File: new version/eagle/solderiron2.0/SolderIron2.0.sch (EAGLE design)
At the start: 7 parts

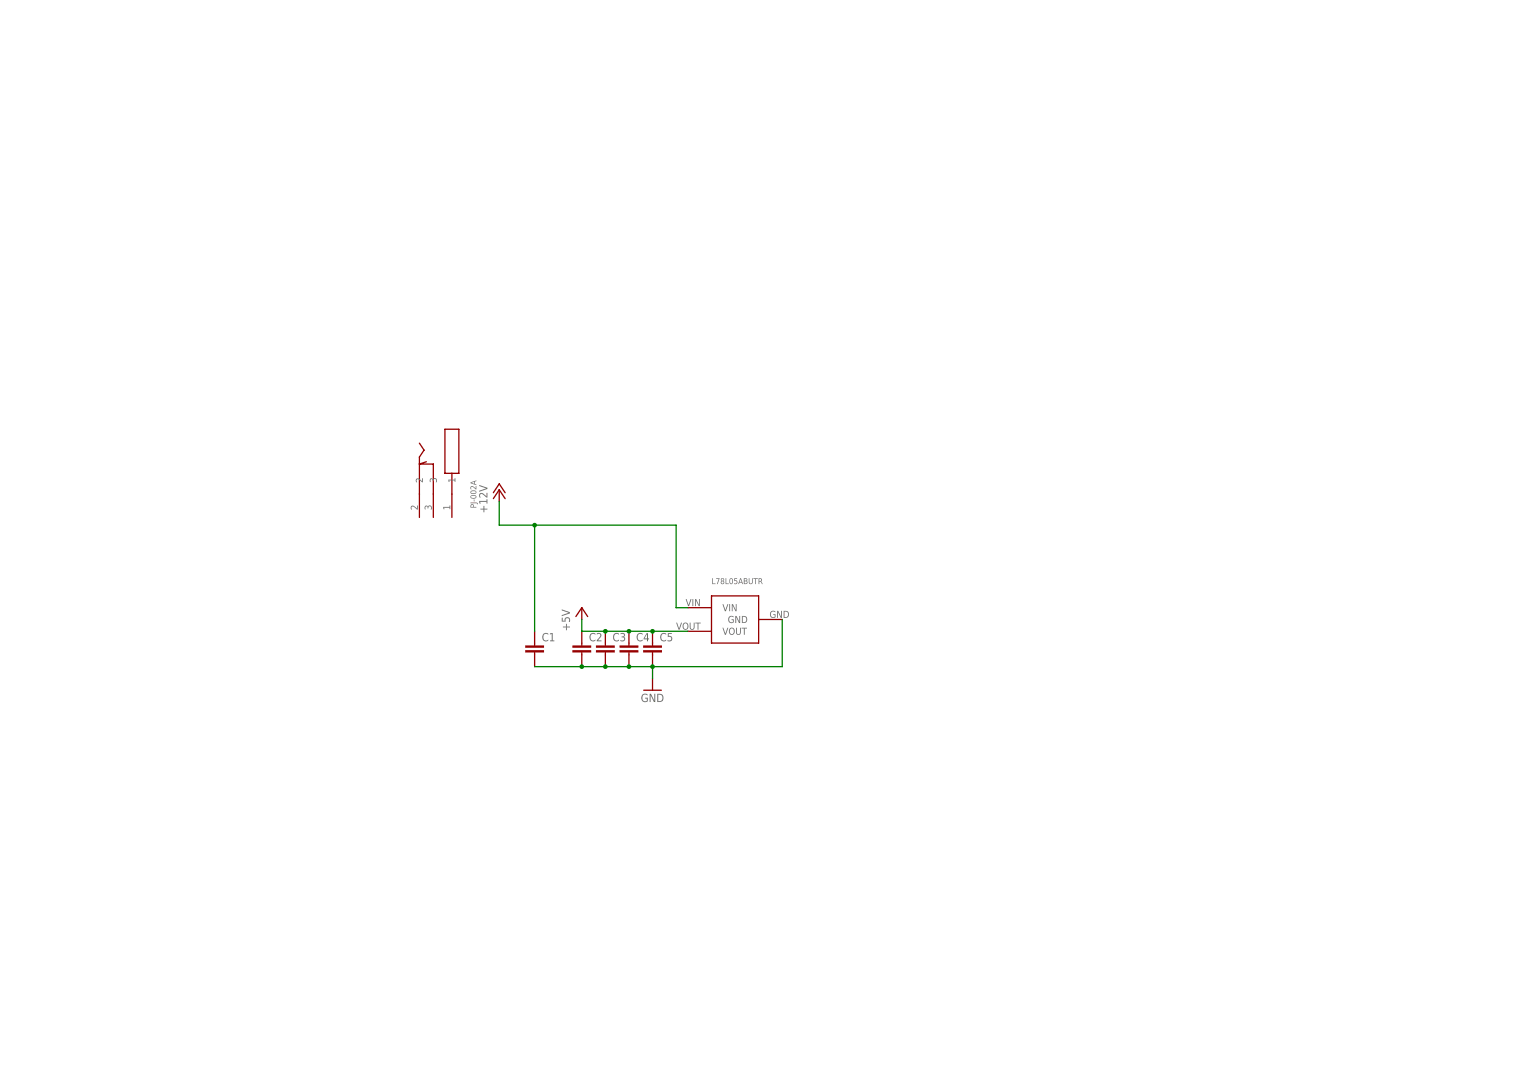
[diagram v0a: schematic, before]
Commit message: created eagle schematics
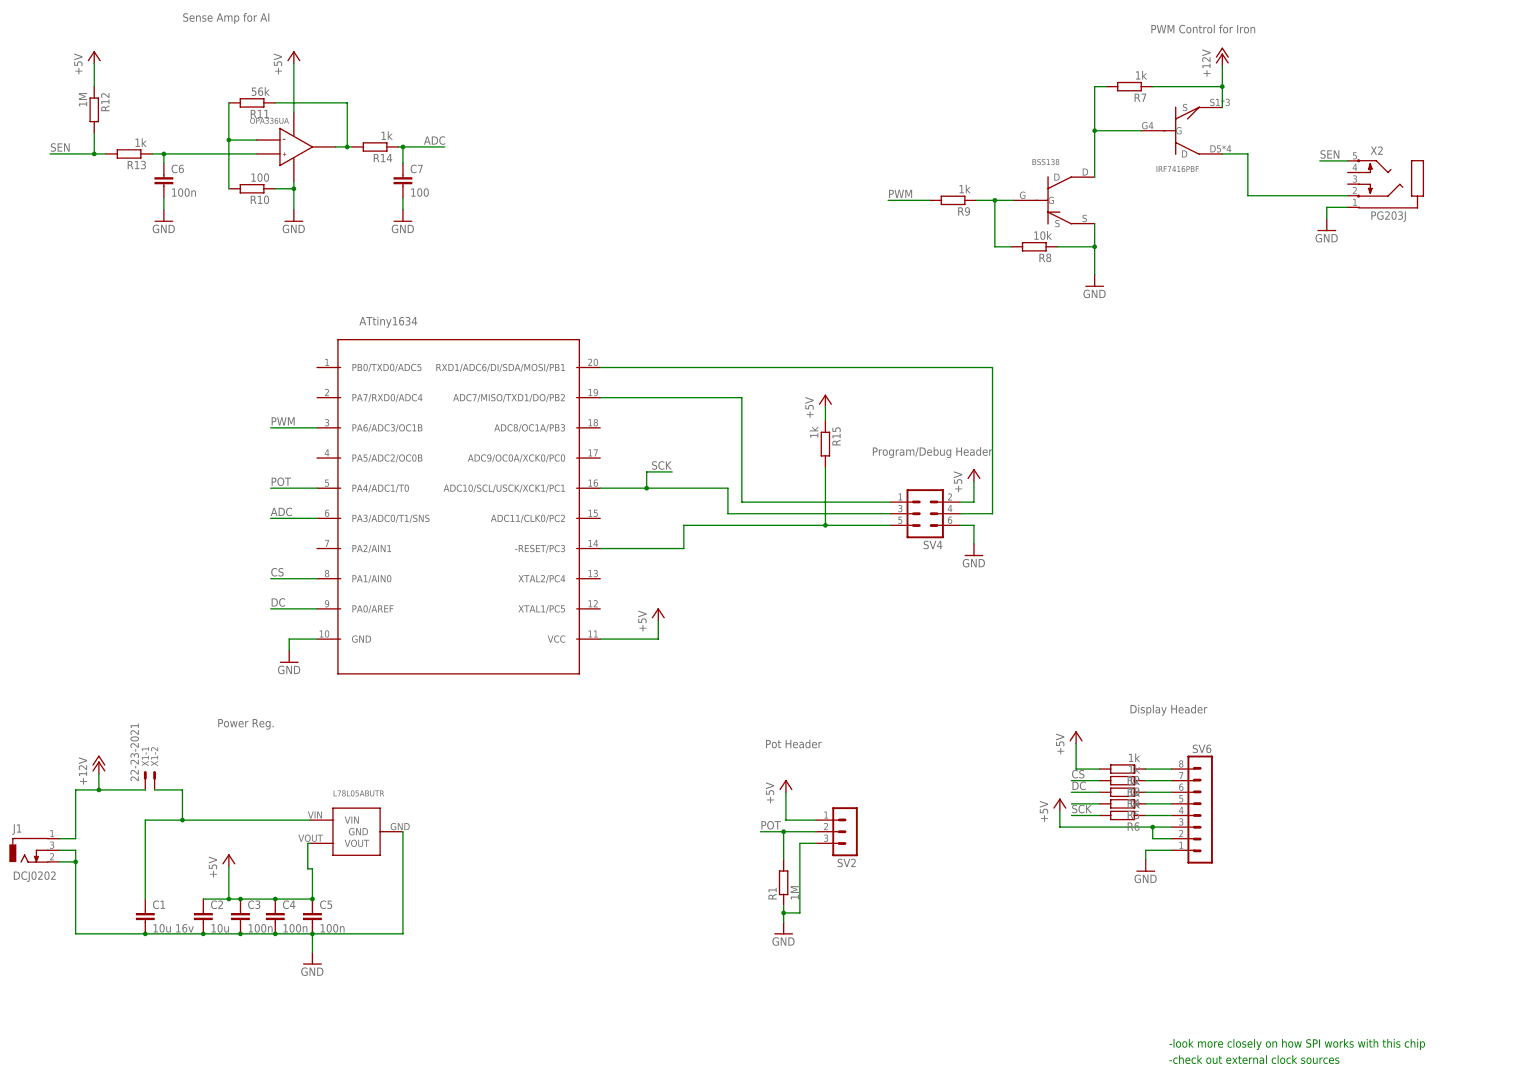
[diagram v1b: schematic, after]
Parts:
- added C6: 100n, eagle-ltspice:CC1206
- added C7: 100, eagle-ltspice:CC1206
- added J1: DCJ0202, solderstation:DCJ0202
- added R1, R12: 1M, eagle-ltspice:RR0603
- added R10: 100, eagle-ltspice:RR0603
- added R11: 56k, eagle-ltspice:RR0603
- added R13, R14, R15, R2, R3, R4, R5, R6, R7, R9: 1k, eagle-ltspice:RR0603
- added R8: 10k, eagle-ltspice:RR0603
- added SV2: (no value), con-lstb:MA03-1
- added SV4: (no value), con-lstb:MA03-2
- added SV6: (no value), con-lstb:MA08-1
- added U$3: BSS138, solderstation:BSS138
- added U$4: OPA336UA, solderstation:OPA336UA
- added U$5: ATTINY1634, solderstation:ATTINY1634
- added X1: 22-23-2021, con-molex:22-23-2021
- added X2: PG203J, solderstation:PG203J
- C1: value (none) -> 10u 16v
- C2: value (none) -> 10u
- C3, C4, C5: value (none) -> 100n
- U$1: value PJ-002A -> IRF7416PBF; device solderstation:PJ-002A -> solderstation:IRF7416PBF
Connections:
- new net ADC: C7.1, R14.1, U$5.PA3/ADC0/T1/SNS
- new net CS: R3.2, U$5.PA1/AIN0
- new net DC: R4.2, U$5.PA0/AREF
- new net MOSI: SV4.1, U$5.ADC7/MISO/TXD1/DO/PB2
- new net N$10: R8.2, R9.1, U$3.G
- new net N$11: R10.2, R11.2, U$4.IN-
- new net N$12: R11.1, R14.2, U$4.OUTPUT
- new net N$13: C6.1, R13.1, U$4.IN+
- new net N$17: SV4.4, U$5.RXD1/ADC6/DI/SDA/MOSI/PB1
- new net N$19: R15.2, SV4.5, U$5.-RESET/PC3
- new net N$2: R2.1, SV6.8
- new net N$23: R5.2
- new net N$3: C1.1, U$2.VIN, X1-2.S
- new net N$4: R3.1, SV6.7
- new net N$5: R4.1, SV6.6
- new net N$6: R5.1, SV6.5
- new net N$7: R6.1, SV6.4
- new net N$8: U$1.D, X2.2
- new net N$9: R7.2, U$1.G, U$3.D
- new net POT: R1.2, SV2.2, U$5.PA4/ADC1/T0
- new net PWM: R9.2, U$5.PA6/ADC3/OC1B
- new net SCK: R6.2, SV4.3, U$5.ADC10/SCL/USCK/XCK1/PC1
- new net SEN: R12.2, R13.2, X2.5
- net +12V: now also J1.1, R7.1, U$1.S; no longer C1.1, U$2.VIN
- net +5V: now also R12.1, R15.1, R2.2, SV2.1, SV4.2, SV6.2, SV6.3, U$4.V+, U$5.VCC
- net GND: now also C6.2, C7.2, J1.2, J1.3, R1.1, R10.1, R8.1, SV2.3, SV4.6, SV6.1, U$3.S, U$4.V-, U$5.GND, X2.1
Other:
- note added: "-check out external clock sources"
- note added: "-look more closely on how SPI works with this chip"
- note added: "Display Header"
- note added: "PWM Control for Iron"
- note added: "Pot Header"
- note added: "Power Reg."
- note added: "Program/Debug Header"
- note added: "Sense Amp for AI"
- moved on the sheet: C1, C2, C3, C4, C5

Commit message: finished v2 schematic
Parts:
- added C8, C9: 22p, eagle-ltspice:CC1206
- added U$6: CX3225GB12000H0KPSC1, solderstation:CX3225GB12000H0KPSC1
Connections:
- removed net N$17: SV4.4, U$5.RXD1/ADC6/DI/SDA/MOSI/PB1
- removed net N$23: R5.2
- new net N$1: C8.1, U$5.XTAL2/PC4, U$6.2
- new net N$14: C9.1, U$5.XTAL1/PC5, U$6.1
- net GND: now also C8.2, C9.2
- net MOSI: now also R5.2, SV4.4, U$5.RXD1/ADC6/DI/SDA/MOSI/PB1
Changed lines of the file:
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@@
 <part name="P+11" library="supply1" deviceset="+5V" device=""/>
 <part name="GND10" library="supply1" deviceset="GND" device=""/>
+<part name="U$6" library="solderstation" deviceset="CX3225GB12000H0KPSC1" device=""/>
+<part name="C8" library="eagle-ltspice" deviceset="C" device="C1206" value="22p"/>
+<part name="C9" library="eagle-ltspice" deviceset="C" device="C1206" value="22p"/>
+<part name="GND11" library="supply1" deviceset="GND" device=""/>
 </parts>
 <sheets>
@@
 <instance part="P+11" gate="1" x="-14" y="-15.5"/>
 <instance part="GND10" gate="1" x="-93.5" y="-27"/>
+<instance part="U$6" gate="G$1" x="9" y="-11.5" rot="R90"/>
+<instance part="C8" gate="G$1" x="28.5" y="-10"/>
+<instance part="C9" gate="G$1" x="22" y="-10"/>
+<instance part="GND11" gate="1" x="25" y="-22.5"/>
 </instances>
 <busses>
@@
 <wire x1="-93.5" y1="-22" x2="-93.5" y2="-24.5" width="0.1524" layer="91"/>
 </segment>
+<segment>
+<pinref part="C9" gate="G$1" pin="2"/>
+<wire x1="22" y1="-15" x2="22" y2="-18" width="0.1524" layer="91"/>
+<pinref part="C8" gate="G$1" pin="2"/>
+<wire x1="22" y1="-18" x2="25" y2="-18" width="0.1524" layer="91"/>
+<wire x1="25" y1="-18" x2="28.5" y2="-18" width="0.1524" layer="91"/>
+<wire x1="28.5" y1="-18" x2="28.5" y2="-15" width="0.1524" layer="91"/>
+<pinref part="GND11" gate="1" pin="GND"/>
+<wire x1="25" y1="-20" x2="25" y2="-18" width="0.1524" layer="91"/>
+<junction x="25" y="-18"/>
+</segment>
 </net>
 <net name="+5V" class="0">
@@
 <wire x1="4" y1="7.5" x2="36" y2="7.5" width="0.1524" layer="91"/>
 </segment>
-</net>
-<net name="N$17" class="0">
 <segment>
 <pinref part="U$5" gate="G$1" pin="RXD1/ADC6/DI/SDA/MOSI/PB1"/>
@@
 <pinref part="SV4" gate="1" pin="4"/>
 <wire x1="58" y1="5" x2="51" y2="5" width="0.1524" layer="91"/>
+<label x="62.5" y="37" size="1.778" layer="95"/>
+<wire x1="58" y1="36.5" x2="67.5" y2="36.5" width="0.1524" layer="91"/>
+<junction x="58" y="36.5"/>
+</segment>
+<segment>
+<pinref part="R5" gate="G$1" pin="2"/>
+<wire x1="81" y1="-57.5" x2="75" y2="-57.5" width="0.1524" layer="91"/>
+<label x="75" y="-57" size="1.778" layer="95"/>
 </segment>
 </net>
@@
 <wire x1="81" y1="-52.5" x2="75" y2="-52.5" width="0.1524" layer="91"/>
 <label x="75" y="-52" size="1.778" layer="95"/>
-</segment>
-</net>
-<net name="N$23" class="0">
-<segment>
-<pinref part="R5" gate="G$1" pin="2"/>
-<wire x1="81" y1="-57.5" x2="75" y2="-57.5" width="0.1524" layer="91"/>
 </segment>
 </net>
@@
 </segment>
 </net>
+<net name="N$1" class="0">
+<segment>
+<pinref part="U$5" gate="G$1" pin="XTAL2/PC4"/>
+<wire x1="-26.5" y1="-9" x2="-3" y2="-9" width="0.1524" layer="91"/>
+<wire x1="-3" y1="-9" x2="-3" y2="-4.5" width="0.1524" layer="91"/>
+<pinref part="U$6" gate="G$1" pin="2"/>
+<wire x1="-3" y1="-4.5" x2="9" y2="-4.5" width="0.1524" layer="91"/>
+<pinref part="C8" gate="G$1" pin="1"/>
+<wire x1="9" y1="-4.5" x2="28.5" y2="-4.5" width="0.1524" layer="91"/>
+<wire x1="28.5" y1="-4.5" x2="28.5" y2="-7.5" width="0.1524" layer="91"/>
+<junction x="9" y="-4.5"/>
+</segment>
+</net>
+<net name="N$14" class="0">
+<segment>
+<pinref part="U$5" gate="G$1" pin="XTAL1/PC5"/>
+<wire x1="-26.5" y1="-15.5" x2="-20.5" y2="-15.5" width="0.1524" layer="91"/>
+<wire x1="-20.5" y1="-15.5" x2="-20.5" y2="-13.5" width="0.1524" layer="91"/>
+<wire x1="-20.5" y1="-13.5" x2="-4.5" y2="-13.5" width="0.1524" layer="91"/>
+<pinref part="U$6" gate="G$1" pin="1"/>
+<wire x1="9" y1="-18.5" x2="-4.5" y2="-18.5" width="0.1524" layer="91"/>
+<wire x1="-4.5" y1="-18.5" x2="-4.5" y2="-13.5" width="0.1524" layer="91"/>
+<wire x1="9" y1="-18.5" x2="14.5" y2="-18.5" width="0.1524" layer="91"/>
+<wire x1="14.5" y1="-18.5" x2="14.5" y2="-7.5" width="0.1524" layer="91"/>
+<junction x="9" y="-18.5"/>
+<pinref part="C9" gate="G$1" pin="1"/>
+<wire x1="14.5" y1="-7.5" x2="22" y2="-7.5" width="0.1524" layer="91"/>
+</segment>
+</net>

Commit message: first board setup
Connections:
- new net N$15: SV4.1, U$5.ADC7/MISO/TXD1/DO/PB2
- net +12V: now also X1-1.S
- net MOSI: no longer SV4.1, U$5.ADC7/MISO/TXD1/DO/PB2
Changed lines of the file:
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@@
 <segment>
 <pinref part="U$5" gate="G$1" pin="VCC"/>
+<pinref part="P+11" gate="1" pin="+5V"/>
 <wire x1="-26.5" y1="-22" x2="-14" y2="-22" width="0.1524" layer="91"/>
 <wire x1="-14" y1="-22" x2="-14" y2="-18" width="0.1524" layer="91"/>
-<pinref part="P+11" gate="1" pin="+5V"/>
 </segment>
 </net>
@@
 <net name="+12V" class="0">
 <segment>
-<wire x1="-124.5" y1="-54.5" x2="-134.5" y2="-54.5" width="0.1524" layer="91"/>
 <wire x1="-134.5" y1="-54.5" x2="-139.5" y2="-54.5" width="0.1524" layer="91"/>
 <wire x1="-139.5" y1="-54.5" x2="-139.5" y2="-65" width="0.1524" layer="91"/>
@@
 <pinref part="P+6" gate="1" pin="+12V"/>
 <wire x1="-134.5" y1="-51" x2="-134.5" y2="-54.5" width="0.1524" layer="91"/>
+<pinref part="X1" gate="-1" pin="S"/>
+<wire x1="-134.5" y1="-54.5" x2="-124.5" y2="-54.5" width="0.1524" layer="91"/>
 <junction x="-134.5" y="-54.5"/>
 </segment>
@@
 </net>
 <net name="MOSI" class="0">
-<segment>
-<pinref part="U$5" gate="G$1" pin="ADC7/MISO/TXD1/DO/PB2"/>
-<wire x1="-26.5" y1="30" x2="4" y2="30" width="0.1524" layer="91"/>
-<wire x1="4" y1="30" x2="4" y2="7.5" width="0.1524" layer="91"/>
-<pinref part="SV4" gate="1" pin="1"/>
-<wire x1="4" y1="7.5" x2="36" y2="7.5" width="0.1524" layer="91"/>
-</segment>
 <segment>
 <pinref part="U$5" gate="G$1" pin="RXD1/ADC6/DI/SDA/MOSI/PB1"/>
@@
 </segment>
 </net>
+<net name="N$15" class="0">
+<segment>
+<pinref part="U$5" gate="G$1" pin="ADC7/MISO/TXD1/DO/PB2"/>
+<wire x1="-26.5" y1="30" x2="10.5" y2="30" width="0.1524" layer="91"/>
+<wire x1="10.5" y1="30" x2="10.5" y2="7.5" width="0.1524" layer="91"/>
+<pinref part="SV4" gate="1" pin="1"/>
+<wire x1="10.5" y1="7.5" x2="36" y2="7.5" width="0.1524" layer="91"/>
+</segment>
+</net>
 </nets>
 </sheet>
 </sheets>
+<errors>
+</errors>
 </schematic>
 </drawing>
